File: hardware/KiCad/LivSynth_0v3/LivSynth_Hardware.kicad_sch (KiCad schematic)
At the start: 0 parts

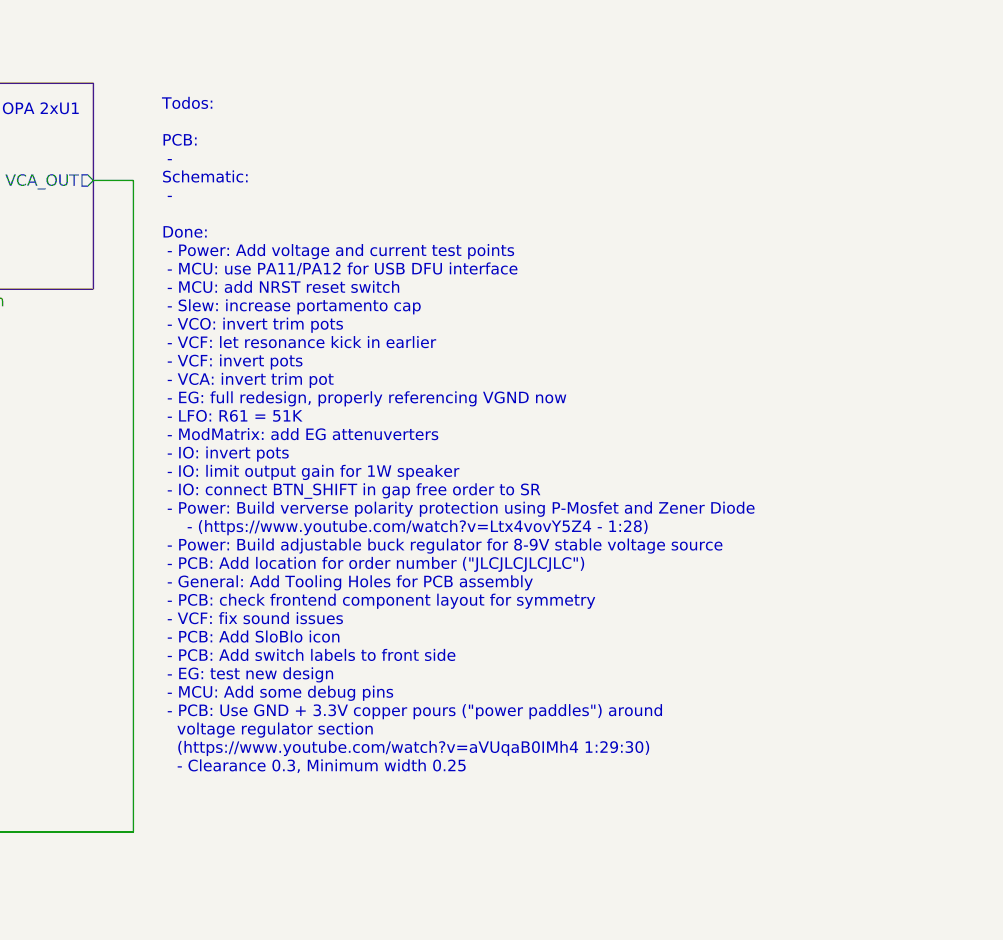
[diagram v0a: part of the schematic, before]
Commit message: Add another LFO cap for easier modding please MCU connectors to the backside Relocate reset button KiCad 7.0.1
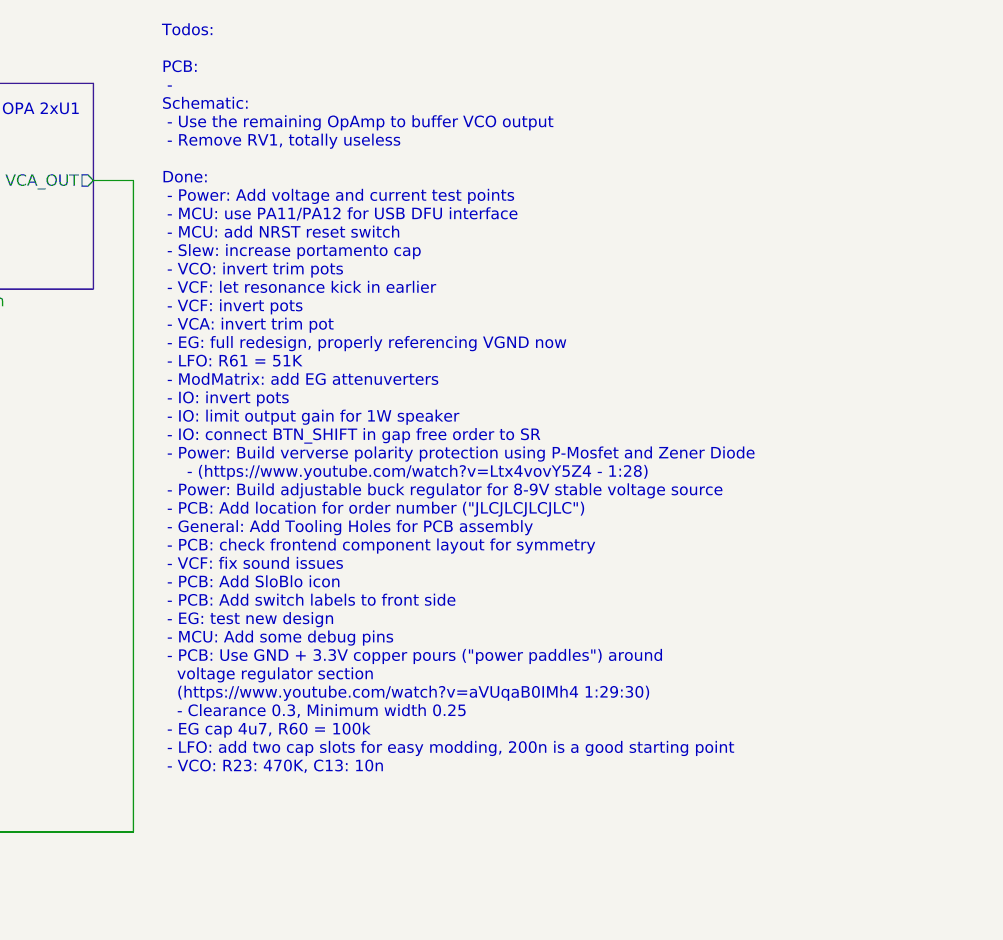
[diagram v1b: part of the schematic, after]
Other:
- note added: "Todos: PCB: - Schematic: - Use the remaining OpAmp to buffer VCO output - Remove RV1, totally useless Done: - Power: Add voltage and current test points - MCU: use PA11/PA12 for USB DFU interface - MCU: add NRST reset switch - Slew: increase portamento cap - VCO: invert trim pots - VCF: let resonance kick in earlier - VCF: invert pots - VCA: invert trim pot - EG: full redesign, properly referenci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"
- note removed: "Todos: PCB: - Schematic: - Done: - Power: Add voltage and current test points - MCU: use PA11/PA12 for USB DFU interface - MCU: add NRST reset switch - Slew: increase portamento cap - VCO: invert trim pots - VCF: let resonance kick in earlier - VCF: invert pots - VCA: invert trim pot - EG: full redesign, properly referencing VGND now - LFO: R61 = 51K - ModMatrix: add EG attenuverters - IO: invert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"

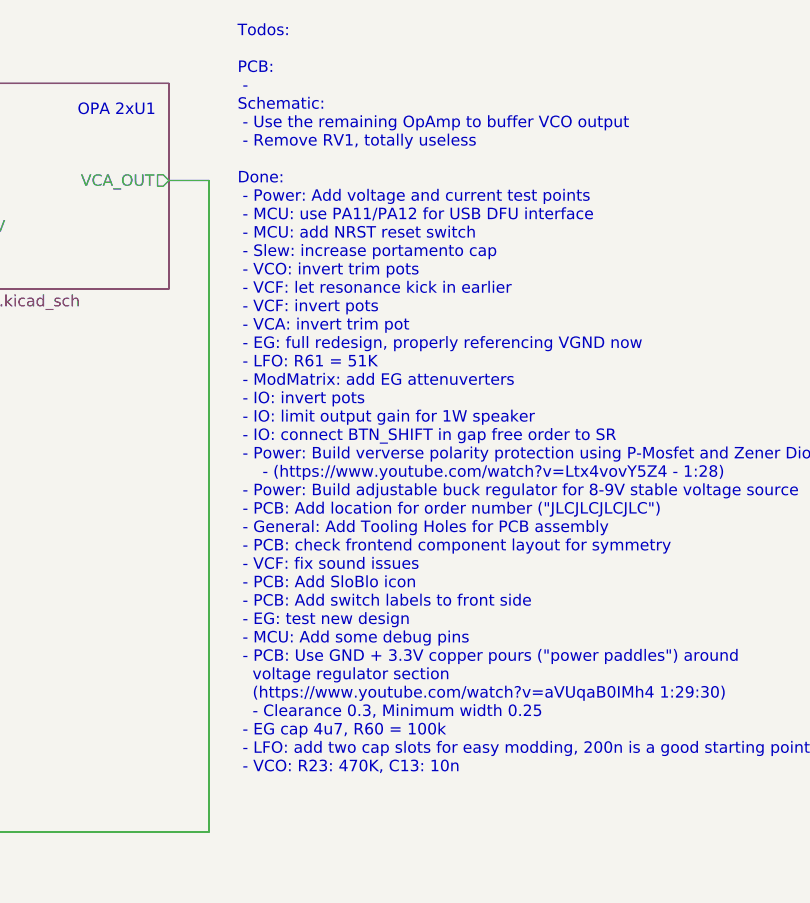
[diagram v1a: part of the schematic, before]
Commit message: RV11 = 100K update BOM RV2 = 100K C13 = 10n R23 = 470K
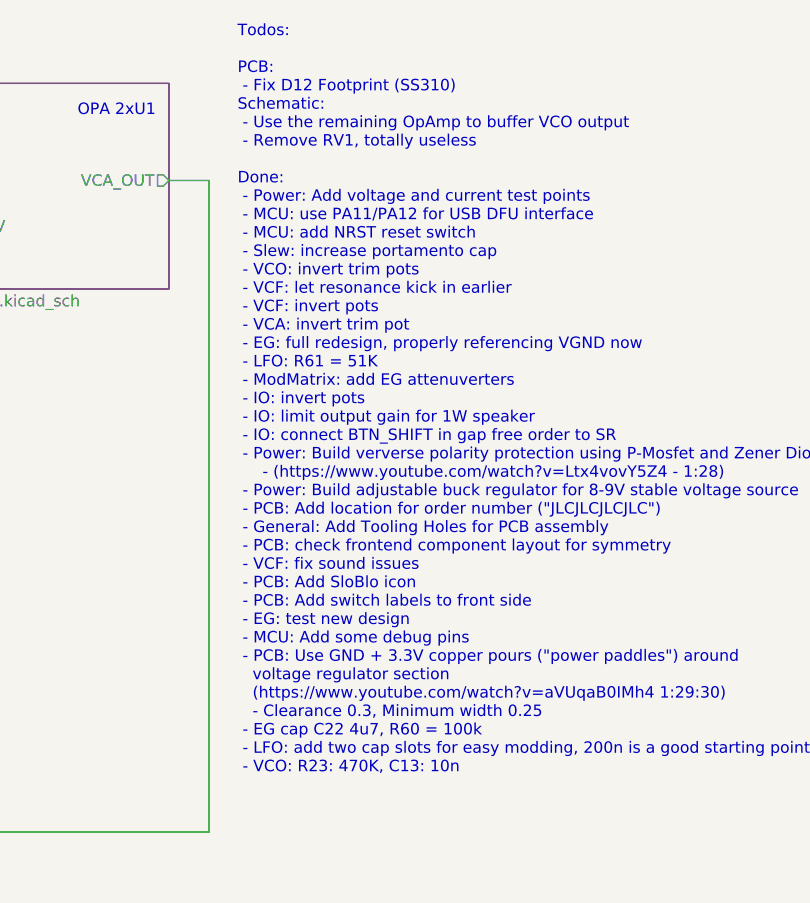
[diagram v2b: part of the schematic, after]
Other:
- note added: "Todos: PCB: - Fix D12 Footprint (SS310) Schematic: - Use the remaining OpAmp to buffer VCO output - Remove RV1, totally useless Done: - Power: Add voltage and current test points - MCU: use PA11/PA12 for USB DFU interface - MCU: add NRST reset switch - Slew: increase portamento cap - VCO: invert trim pots - VCF: let resonance kick in earlier - VCF: invert pots - VCA: invert trim pot - EG: full re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"
- note removed: "Todos: PCB: - Schematic: - Use the remaining OpAmp to buffer VCO output - Remove RV1, totally useless Done: - Power: Add voltage and current test points - MCU: use PA11/PA12 for USB DFU interface - MCU: add NRST reset switch - Slew: increase portamento cap - VCO: invert trim pots - VCF: let resonance kick in earlier - VCF: invert pots - VCA: invert trim pot - EG: full redesign, properly referenci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"
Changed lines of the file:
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@@
     (effects (font (size 1.27 1.27)) (justify left bottom))
   )
-  (text "Todos:\n\nPCB:\n - \nSchematic:\n - Use the remaining OpAmp to buffer VCO output\n - Remove RV1, totally useless\n\nDone:\n - Power: Add voltage and current test points\n - MCU: use PA11/PA12 for USB DFU interface\n - MCU: add NRST reset switch\n - Slew: increase portamento cap\n - VCO: invert trim pots\n - VCF: let resonance kick in earlier\n - VCF: invert pots\n - VCA: invert trim pot\n - EG: full redesign, properly referencing VGND now\n - LFO: R61 = 51K\n - ModMatrix: add EG attenuverters\n - IO: invert pots\n - IO: limit output gain for 1W speaker\n - IO: connect BTN_SHIFT in gap free order to SR\n - Power: Build ververse polarity protection using P-Mosfet and Zener Diode\n     - (https://www.youtube.com/watch?v=Ltx4vovY5Z4 - 1:28)\n - Power: Build adjustable buck regulator for 8-9V stable voltage source\n - PCB: Add location for order number (\"JLCJLCJLCJLC\")\n - General: Add Tooling Holes for PCB assembly\n - PCB: check frontend component layout for symmetry\n - VCF: fix sound issues\n - PCB: Add SloBlo icon\n - PCB: Add switch labels to front side\n - EG: test new design\n - MCU: Add some debug pins\n - PCB: Use GND + 3.3V copper pours (\"power paddles\") around\n   voltage regulator section\n   (https://www.youtube.com/watch?v=aVUqaB0IMh4 1:29:30)\n   - Clearance 0.3, Minimum width 0.25\n - EG cap 4u7, R60 = 100k\n - LFO: add two cap slots for easy modding, 200n is a good starting point\n - VCO: R23: 470K, C13: 10n"
+  (text "Todos:\n\nPCB:\n - Fix D12 Footprint (SS310)\nSchematic:\n - Use the remaining OpAmp to buffer VCO output\n - Remove RV1, totally useless\n\nDone:\n - Power: Add voltage and current test points\n - MCU: use PA11/PA12 for USB DFU interface\n - MCU: add NRST reset switch\n - Slew: increase portamento cap\n - VCO: invert trim pots\n - VCF: let resonance kick in earlier\n - VCF: invert pots\n - VCA: invert trim pot\n - EG: full redesign, properly referencing VGND now\n - LFO: R61 = 51K\n - ModMatrix: add EG attenuverters\n - IO: invert pots\n - IO: limit output gain for 1W speaker\n - IO: connect BTN_SHIFT in gap free order to SR\n - Power: Build ververse polarity protection using P-Mosfet and Zener Diode\n     - (https://www.youtube.com/watch?v=Ltx4vovY5Z4 - 1:28)\n - Power: Build adjustable buck regulator for 8-9V stable voltage source\n - PCB: Add location for order number (\"JLCJLCJLCJLC\")\n - General: Add Tooling Holes for PCB assembly\n - PCB: check frontend component layout for symmetry\n - VCF: fix sound issues\n - PCB: Add SloBlo icon\n - PCB: Add switch labels to front side\n - EG: test new design\n - MCU: Add some debug pins\n - PCB: Use GND + 3.3V copper pours (\"power paddles\") around\n   voltage regulator section\n   (https://www.youtube.com/watch?v=aVUqaB0IMh4 1:29:30)\n   - Clearance 0.3, Minimum width 0.25\n - EG cap C22 4u7, R60 = 100k\n - LFO: add two cap slots for easy modding, 200n is a good starting point\n - VCO: R23: 470K, C13: 10n"
     (at 212.09 99.695 0)
     (effects (font (size 1.27 1.27)) (justify left bottom))
